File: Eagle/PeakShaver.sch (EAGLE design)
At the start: 19 parts, among them J1 A5V, J2 SM5V, J3 RJ11, J4 RGB Button, T1 BC547, X4 RS485

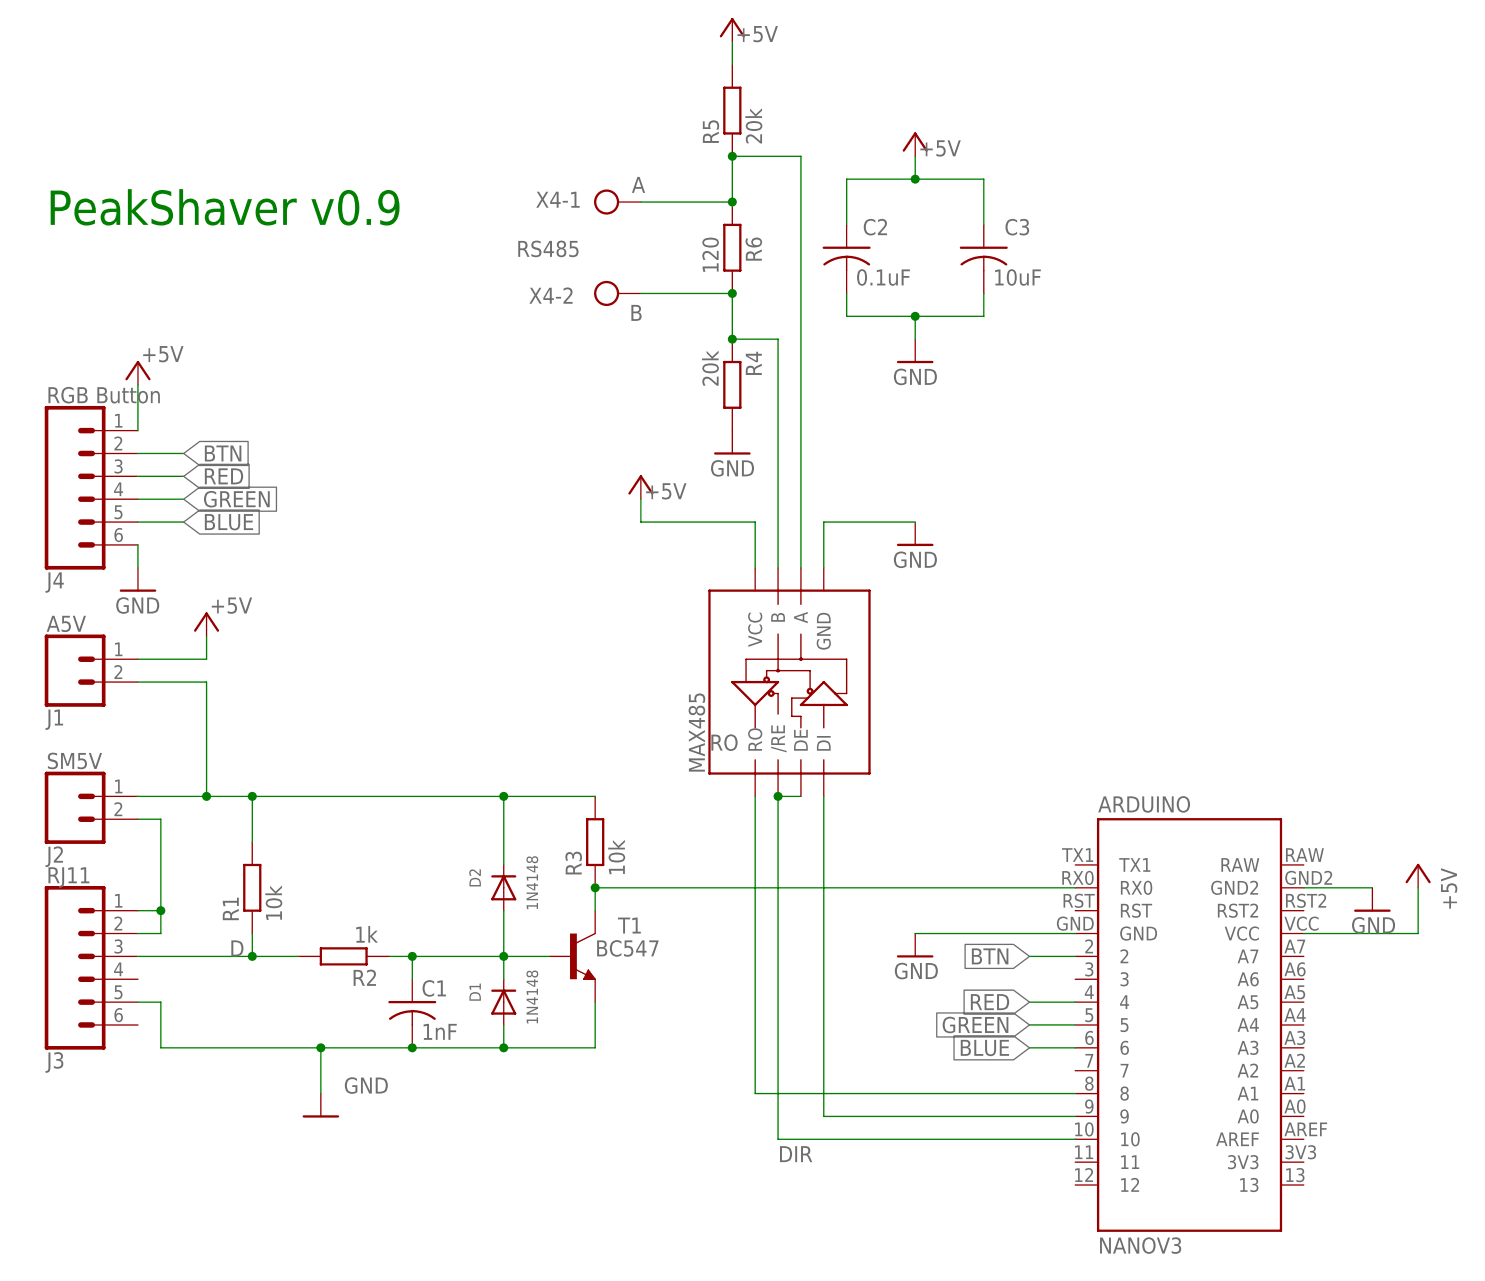
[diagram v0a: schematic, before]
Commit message: fixed bug in P1 connection
P1 ground and data line were swapped in version 0.9
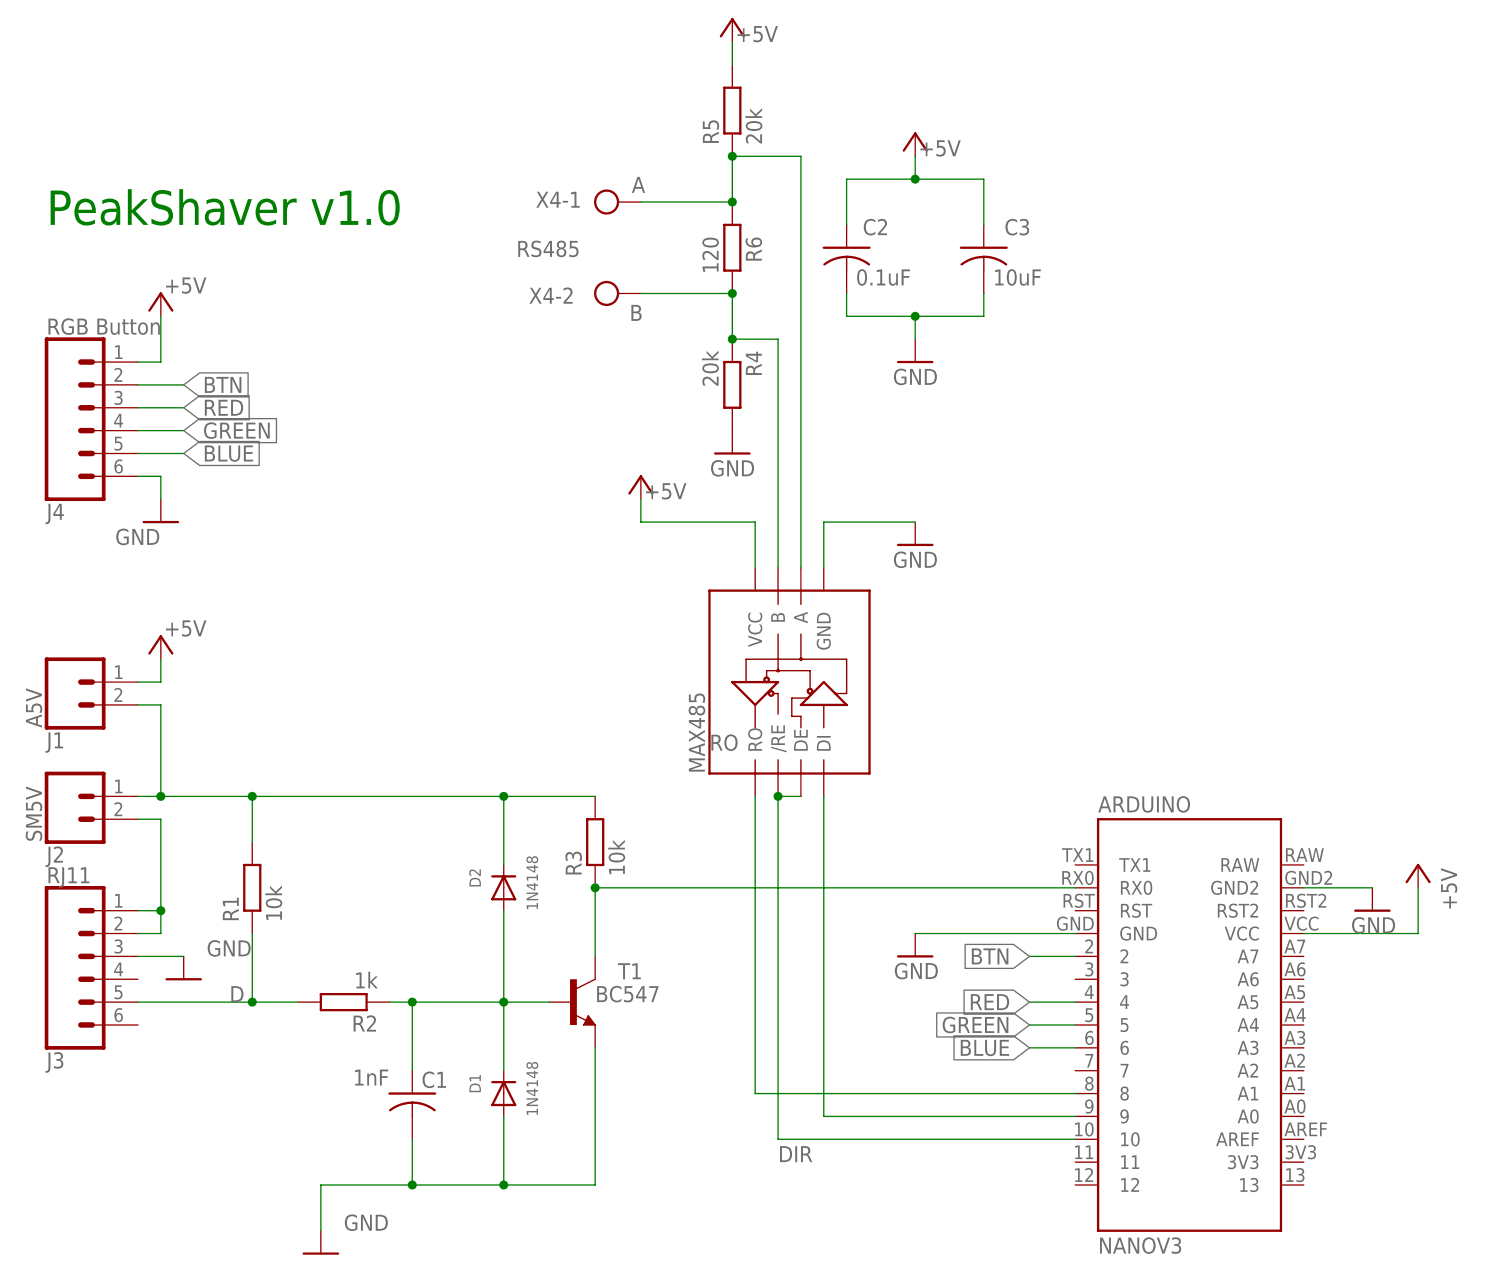
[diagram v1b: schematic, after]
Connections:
- net D: now also J3.5; no longer J3.3
- net GND: now also J3.3; no longer J3.5
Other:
- note added: "PeakShaver v1.0"
- note removed: "PeakShaver v0.9"
- moved on the sheet: C1, D1, J1, J4, R2, T1
